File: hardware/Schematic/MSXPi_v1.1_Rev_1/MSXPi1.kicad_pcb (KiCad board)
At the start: 2 copper layers, 102.6 x 65.3 mm, 48 parts, among them J1 Raspberry_Pi_Zero_2_3, J3 Conn_02x07_Odd_Even, J4 Conn_02x06_Odd_Even, P1 MSX_CONNECTOR

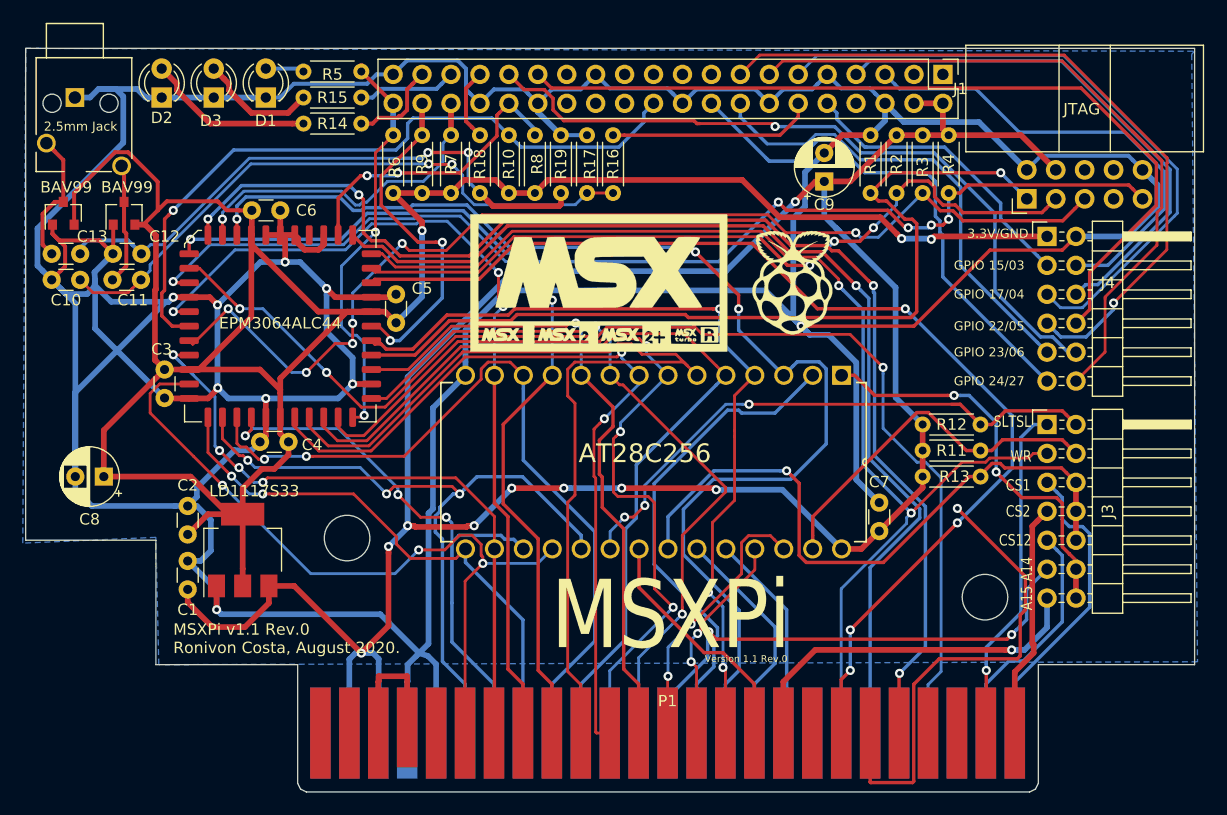
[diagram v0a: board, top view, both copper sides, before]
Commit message: Changed CPLD foot print
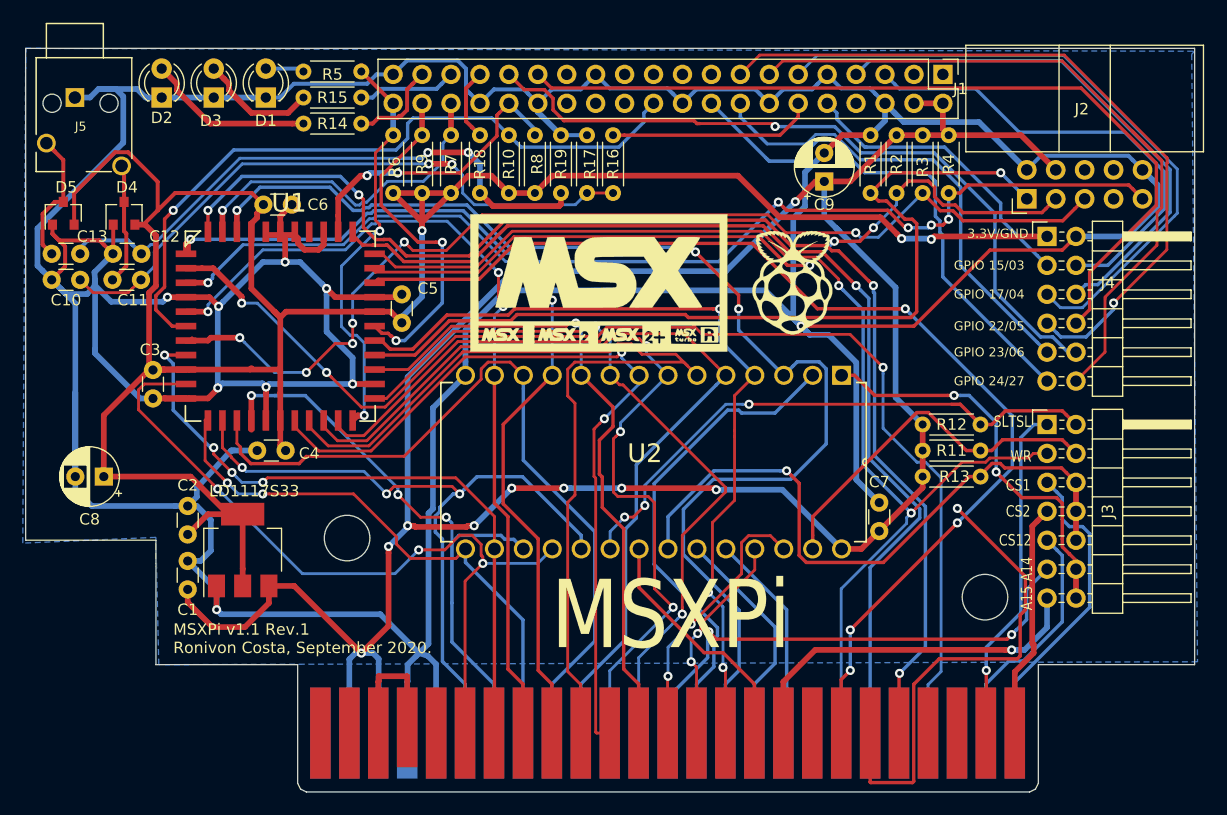
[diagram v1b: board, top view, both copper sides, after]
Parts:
- J5: renamed from 2.5mm Jack
- U1: renamed from EPM3064ALC44; footprint MyFootprints:PLCC-44_16.6x16.6mm_P1.27mm -> MyFootprints:PLCC127P1765X1765X457-44N
- moved C6 1.14 mm to (118.1, 81.3)
- moved C3 1.02 mm to (105.9, 98.3)
- moved C4 0.80 mm to (115.1, 102.9)
- moved C5 0.51 mm to (127.8, 89.2)
- renumbered BAV99 to D4, BAV99 to D5, JTAG to J2, AT28C256 to U2
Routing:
- net +3V3: track 222.4 -> 212.0 mm
- net GNDREF: track 508.1 -> 500.7 mm
- net D5: track 56.3 -> 59.6 mm
- net SPI_MISO: track 27.6 -> 30.5 mm
- net D0: track 81.7 -> 79.3 mm
- net D2: track 77.1 -> 74.9 mm
- net D6: track 66.0 -> 68.1 mm
- net SPI_CS: track 36.0 -> 37.7 mm
- net TDI: track 94.3 -> 95.7 mm
- net TMS: track 95.4 -> 94.3 mm
- net BUSDIR: track 111.1 -> 112.1 mm
- net D3: track 48.5 -> 49.3 mm
- net D4: track 59.5 -> 58.8 mm
- net D1: track 68.1 -> 68.8 mm, vias 2 -> 0
- net WAIT: track 105.5 -> 106.1 mm
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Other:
- board text added: "MSXPi v1.1 Rev.1 Ronivon Costa, September 2020."
- board text removed: "MSXPi v1.1 Rev.0 Ronivon Costa, August 2020."
- board text removed: "Version 1.1 Rev.0"
